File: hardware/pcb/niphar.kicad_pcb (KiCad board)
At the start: 4 copper layers, 340.8 x 104.7 mm, 287 parts, among them J1 Conn_02x03_Odd_Even, J10 Battery, J11 Battery, J12 Conn_01x05_Pin, J2 Conn_02x03_Odd_Even, J3 TPS43_FPC, J4 Conn_01x05_Pin, J5 AudioJack4, J6 AudioJack4, J7 USB_C_Receptacle_USB2.0_16P, J8 USB_C_Receptacle_USB2.0_16P, J9 Micro_SD_Card, Q1 AO3407, Q2 AO3407, Q3 FS8205, Q4 FS8205, SW1 SW_PUSH, SW10 SW_PUSH, SW11 SW_PUSH, SW12 SW_PUSH, SW13 SW_PUSH, SW14 SW_PUSH, SW15 SW_PUSH, SW16 SW_PUSH, SW17 SW_PUSH, SW18 SW_PUSH, SW19 SW_PUSH, SW2 SW_PUSH, SW20 SW_PUSH, SW21 SW_PUSH, SW22 SW_PUSH, SW23 SW_PUSH, SW24 SW_PUSH, SW25 SW_PUSH, SW26 SW_PUSH, SW27 SW_PUSH, SW28 SW_PUSH, SW29 SW_PUSH, SW3 SW_PUSH, SW30 SW_PUSH, SW31 SW_PUSH, SW32 SW_PUSH, SW33 SW_PUSH, SW34 SW_PUSH, SW35 SW_PUSH, SW36 SW_PUSH, SW37 SW_PUSH, SW38 SW_PUSH, SW39 SW_PUSH, SW4 SW_PUSH, SW40 SW_PUSH, SW41 SW_PUSH, SW42 SW_PUSH, SW43 SW_PUSH, SW44 SW_PUSH, SW45 SW_PUSH, SW46 SW_PUSH, SW47 SW_PUSH, SW48 SW_PUSH, SW49 SW_PUSH, SW5 SW_PUSH, SW50 SW_PUSH, SW51 SW_PUSH, SW52 SW_PUSH, SW53 SW_SPDT, SW54 SW_SPDT, SW6 SW_PUSH, SW7 SW_PUSH, SW8 SW_PUSH, SW9 SW_PUSH, U1 D, U10 SRV05-4, U11 SiP32431DR3, U12 SiP32431DR3, U13 CH334R, U14 USBLC6-2SC6, U15 USBLC6-2SC6, U16 ESP32P4_QFN104, U17 AMS1117-3.3, U18 TP4056-42-ESOP8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

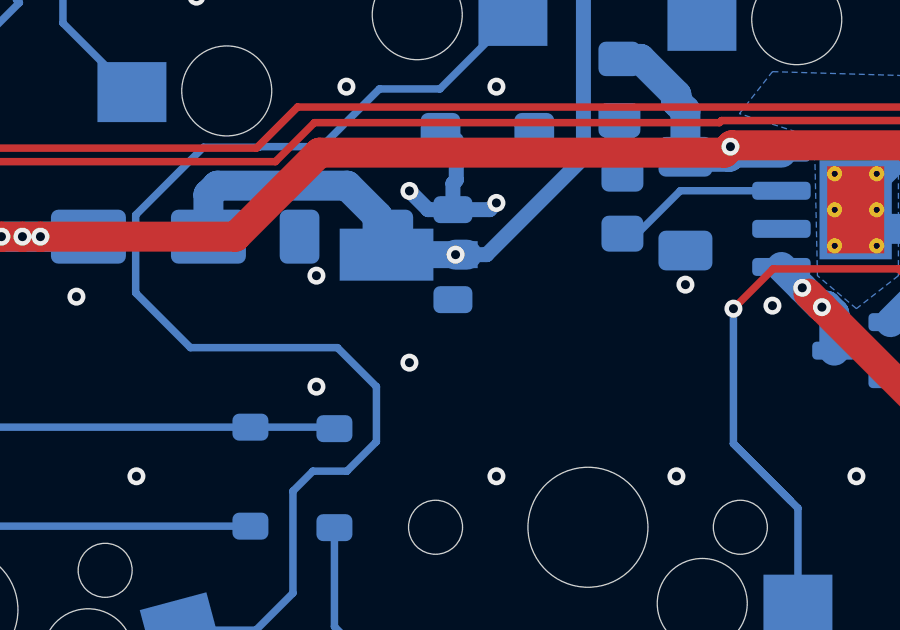
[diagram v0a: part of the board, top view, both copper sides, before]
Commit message: C23 deplace + liste de commande des composants actifs
C23 (10uF, 1206, B.Cu) passe de (266,83 . 76,38) a (275,06 . 80,28), tourne
de 90 degres.

order-lcsc-actifs.csv entre au depot : la liste des references LCSC des
composants actifs, avec les quantites par moitie et par carte. Deux lignes
restent en "A CHOISIR" (LED temoin de charge, LED infrarouge du capteur) — la
seconde est a supprimer plutot qu'a remplir, le PMW3360 embarquant sa propre
LED IR (voir Conchodytes, NOTES-V2.md point 6).

Le reordonnancement de used_designators dans le .pro et le .prl sont du bruit
de session KiCad.

Co-Authored-By: Claude Opus 5 (1M context) <noreply@anthropic.com>
Claude-Session: https://claude.ai/code/session_01DronP1g7SanVhLombKppxw
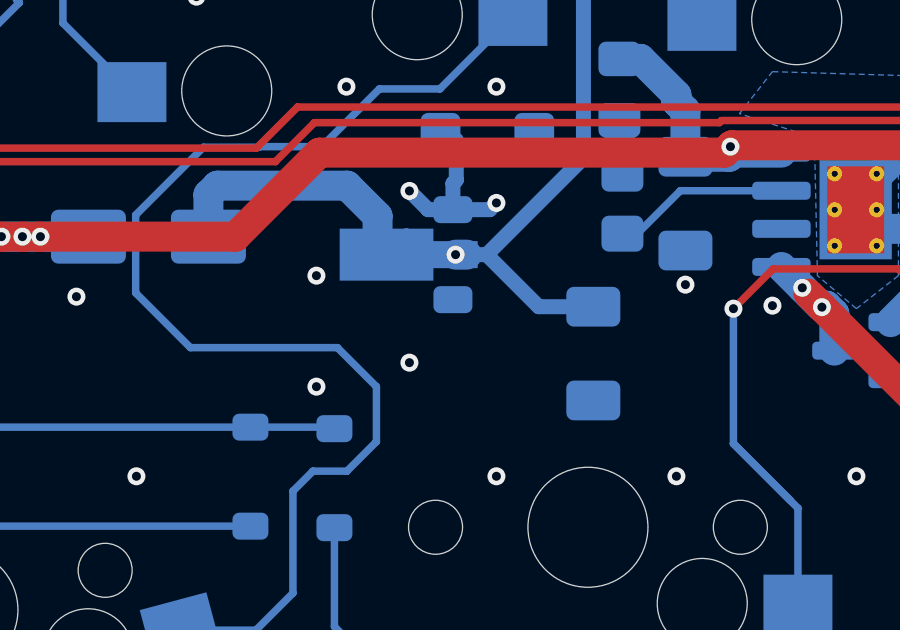
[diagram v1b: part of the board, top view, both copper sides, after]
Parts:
- moved C23 9.11 mm to (275.1, 80.3), turned to 90 degrees
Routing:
- net Net-(D51-K): track 109.7 -> 113.9 mm
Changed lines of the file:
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@@
 	(footprint "Capacitor_SMD:C_1206_3216Metric_Pad1.33x1.80mm_HandSolder"
 		(layer "B.Cu")
-		(at 266.830708 76.384853)
+		(at 275.06048 80.283 90)
 		(descr "Capacitor SMD 1206 (3216 Metric), square (rectangular) end terminal, IPC-7351 nominal with elongated pad for handsoldering. (Body size source: IPC-SM-782 page 76, https://www.pcb-3d.com/wordpress/wp-content/uploads/ipc-sm-782a_amendment_1_and_2.pdf)")
 		(tags "capacitor handsolder")
 		(property "Reference" "C23"
-			(at 0 1.85 0)
+			(at 0 1.85 90)
 			(layer "B.SilkS")
 			(hide yes)
@@
 		)
 		(property "Value" "10uF"
-			(at 0 -1.85 0)
+			(at 0 -1.85 90)
 			(layer "B.Fab")
 			(effects
@@
 		)
 		(property "Datasheet" ""
-			(at 0 0 0)
+			(at 0 0 90)
 			(layer "B.Fab")
 			(hide yes)
@@
 		)
 		(property "Description" "Unpolarized capacitor"
-			(at 0 0 0)
+			(at 0 0 90)
 			(layer "B.Fab")
 			(hide yes)
@@
 		)
 		(property "KiLib_Generator" "SMD_2terminal_chip_molded"
-			(at 0 0 0)
+			(at 0 0 90)
 			(layer "B.SilkS")
 			(hide yes)
@@
 		)
 		(fp_text user "${REFERENCE}"
-			(at 0 0 0)
+			(at 0 0 90)
 			(layer "B.Fab")
 			(effects
@@
 		)
 		(pad "1" smd roundrect
-			(at -1.5625 0 180)
+			(at -1.5625 0 270)
 			(size 1.325 1.8)
 			(layers "B.Cu" "B.Mask" "B.Paste")
@@
 		)
 		(pad "2" smd roundrect
-			(at 1.5625 0 180)
+			(at 1.5625 0 270)
 			(size 1.325 1.8)
 			(layers "B.Cu" "B.Mask" "B.Paste")
@@
 	(segment
 		(start 271.506188 76.984853)
+		(end 273.241835 78.7205)
+		(width 0.5)
+		(layer "B.Cu")
+		(net "Net-(D51-K)")
+	)
+	(segment
+		(start 271.506188 76.984853)
 		(end 270.468208 76.984853)
 		(width 0.5)
@@
 		(width 0.5)
 		(layer "B.Cu")
+		(net "Net-(D51-K)")
+	)
+	(segment
+		(start 273.241835 78.7205)
+		(end 275.06048 78.7205)
+		(width 0.5)
+		(layer "B.Cu")
